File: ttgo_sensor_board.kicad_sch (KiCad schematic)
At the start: 56 parts, among them J1 Conn_01x13_Female, J2 Conn_01x13_Female, J3 Conn_01x03_Female, J4 Conn_01x03_Female, J5 Conn_01x04_Female, J6 Conn_01x04_Female, J7 Conn_01x04_Female, Q1 Q_NMOS_GSD, Q2 Q_NMOS_GSD, U1 BME680, U2 TCA9800, U3 TLV70218_SOT23-5, U4 LSM6DS3, U5 VEML7700

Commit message: backup current state
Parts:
- added TP12, TP13: TestPoint, TestPoint:TestPoint_Pad_D1.0mm, symbol Connector:TestPoint
- D3: value USER0 -> U0
- D4: value USER1 -> U1
- R2: value 290 -> 294
- TP1, TP2, TP3, TP4, TP5, TP6, TP7: footprint TestPoint:TestPoint_Pad_D1.5mm -> TestPoint:TestPoint_Pad_D1.0mm
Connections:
- net GND: no longer J2.11 (Pin_11)
- net GPIO34: now also TP12.1
- net GPIO35: now also TP13.1
- net GPIO36: no longer TP2.1
- net GPIO39: no longer TP3.1
- net VCC5: no longer J2.12 (Pin_12)
- net at Q2.3 (D), R8.1: now also TP3.1
- net at Q1.3 (D), R7.1: now also TP2.1
- new net GPIO00: J2.11 (Pin_11)
- new net GPIO04: J2.12 (Pin_12)
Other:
- moved on the sheet: TP2, TP3

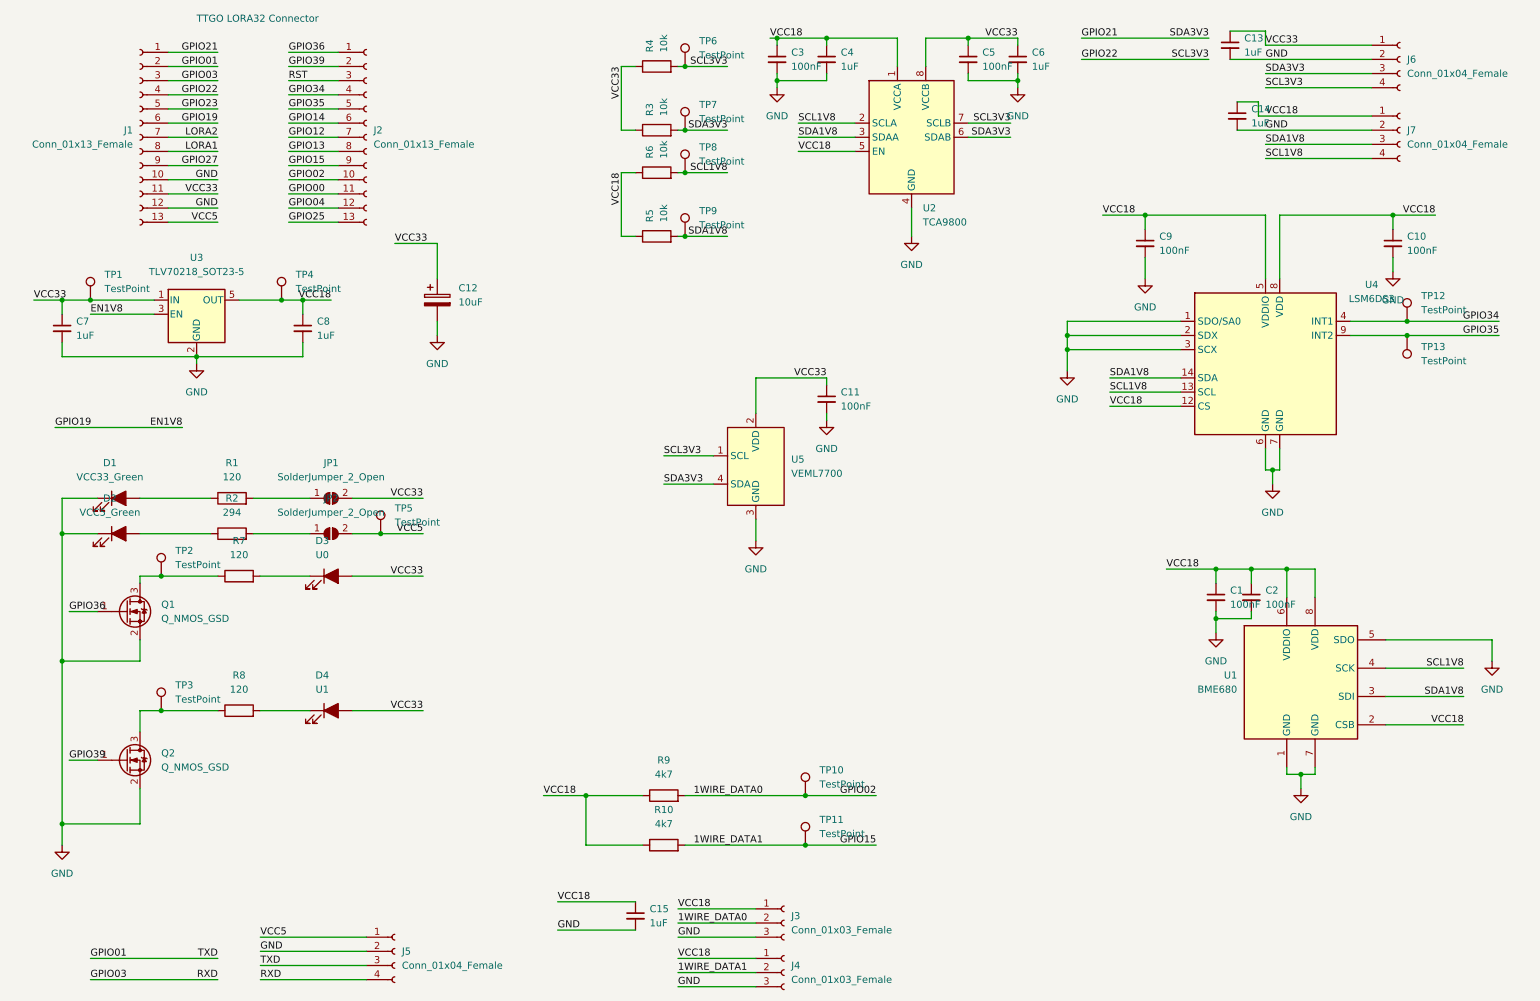
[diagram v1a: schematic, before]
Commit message: moved leds and change silkscreen
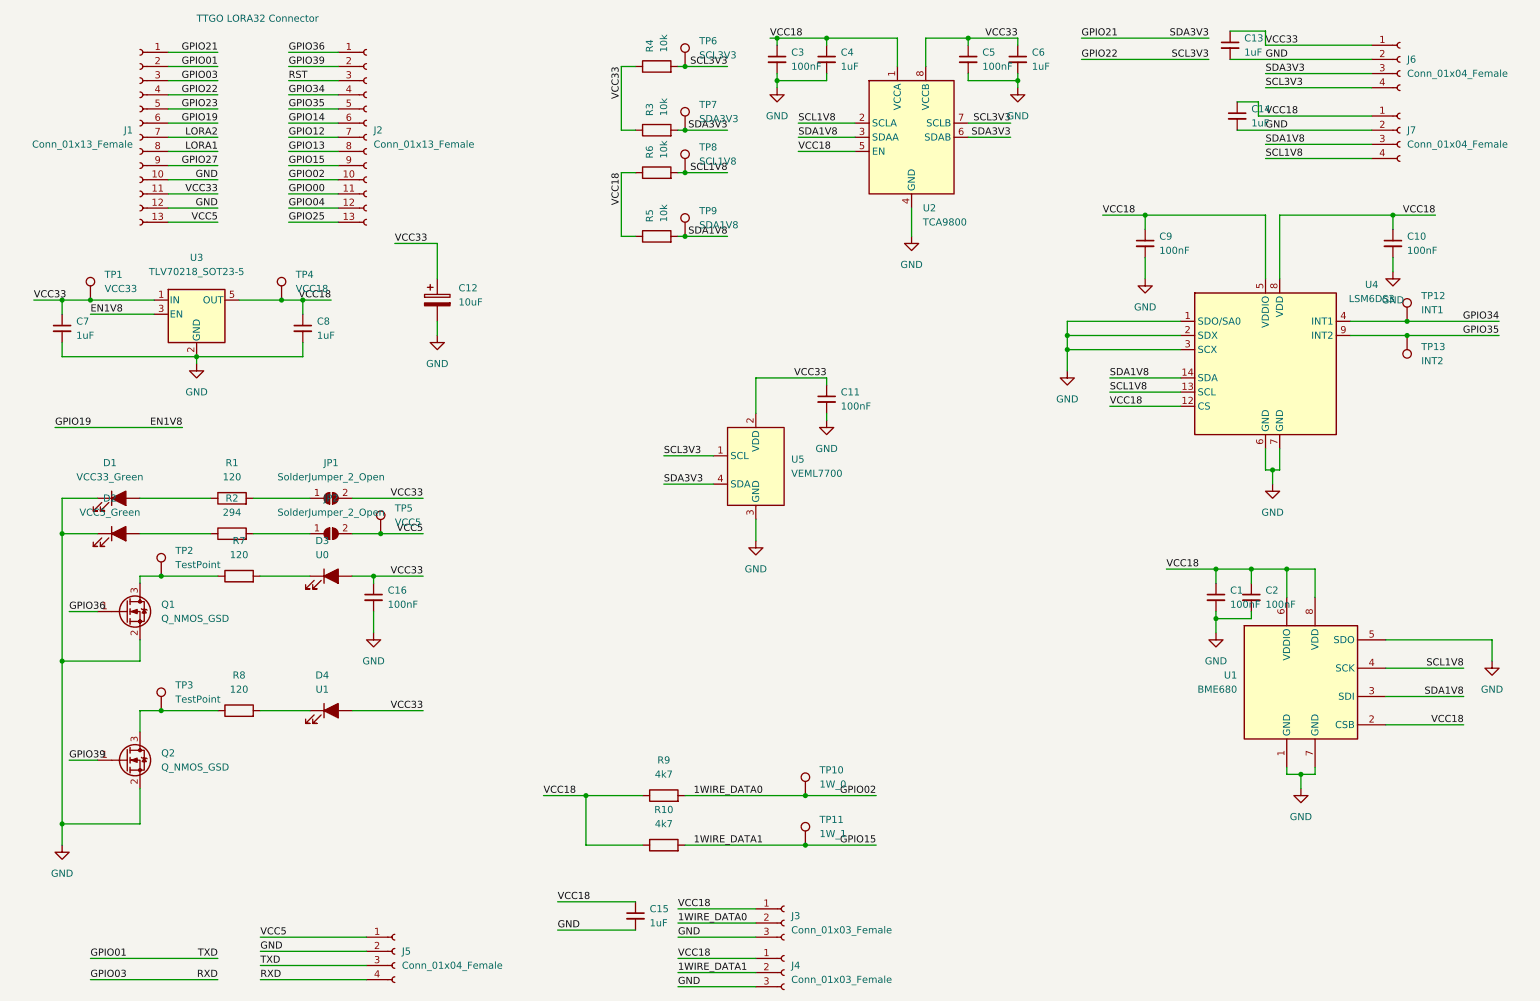
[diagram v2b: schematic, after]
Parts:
- added C16: 100nF, Capacitor_SMD:C_0603_1608Metric, symbol Device:C_Small
- TP1: value TestPoint -> VCC33
- TP10: value TestPoint -> 1W_0
- TP11: value TestPoint -> 1W_1
- TP12: value TestPoint -> INT1
- TP13: value TestPoint -> INT2
- TP4: value TestPoint -> VCC18
- TP5: value TestPoint -> VCC5
- TP6: value TestPoint -> SCL3V3
- TP7: value TestPoint -> SDA3V3
- TP8: value TestPoint -> SCL1V8
- TP9: value TestPoint -> SDA1V8
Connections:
- net GND: now also C16.2
- net VCC33: now also C16.1
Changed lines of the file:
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@@
   (junction (at 261.62 53.34) (diameter 0) (color 0 0 0 0)
   )
+  (junction (at 78.74 118.11) (diameter 0) (color 0 0 0 0)
+  )
   (junction (at 240.03 99.06) (diameter 0) (color 0 0 0 0)
   )
@@
     (stroke (width 0) (type default) (color 0 0 0 0))
   )
+  (wire (pts (xy 78.74 118.11) (xy 87.63 118.11))
+    (stroke (width 0) (type default) (color 0 0 0 0))
+  )
   (wire (pts (xy 247.65 152.4) (xy 247.65 153.67))
     (stroke (width 0) (type default) (color 0 0 0 0))
@@
     (stroke (width 0) (type default) (color 0 0 0 0))
   )
-  (wire (pts (xy 74.93 118.11) (xy 87.63 118.11))
+  (wire (pts (xy 74.93 118.11) (xy 78.74 118.11))
     (stroke (width 0) (type default) (color 0 0 0 0))
   )
@@
     (stroke (width 0) (type default) (color 0 0 0 0))
   )
+  (wire (pts (xy 78.74 118.11) (xy 78.74 119.38))
+    (stroke (width 0) (type default) (color 0 0 0 0))
+  )
   (wire (pts (xy 245.11 153.67) (xy 242.57 153.67))
     (stroke (width 0) (type default) (color 0 0 0 0))
@@
   )
   (wire (pts (xy 217.17 53.34) (xy 217.17 55.88))
+    (stroke (width 0) (type default) (color 0 0 0 0))
+  )
+  (wire (pts (xy 78.74 124.46) (xy 78.74 128.27))
     (stroke (width 0) (type default) (color 0 0 0 0))
   )
@@
     (pin "1")
     (pin "2")
+  )
+  (symbol (lib_id "power:GND") (at 78.74 128.27 0) (unit 1)
+    (in_bom yes) (on_board yes) (fields_autoplaced)
+    (property "Reference" "#PWR016" (id 0) (at 78.74 134.62 0)
+      (effects (font (size 1.27 1.27)) hide)
+    )
+    (property "Value" "GND" (id 1) (at 78.74 133.35 0))
+    (property "Footprint" "" (id 2) (at 78.74 128.27 0)
+      (effects (font (size 1.27 1.27)) hide)
+    )
+    (property "Datasheet" "" (id 3) (at 78.74 128.27 0)
+      (effects (font (size 1.27 1.27)) hide)
+    )
+    (pin "1")
   )
   (symbol (lib_id "Device:R") (at 129.54 45.72 90) (unit 1)
@@
       (effects (font (size 1.27 1.27)) (justify left))
     )
-    (property "Value" "TestPoint" (id 1) (at 158.75 155.4479 0)
+    (property "Value" "1W_0" (id 1) (at 158.75 155.4479 0)
       (effects (font (size 1.27 1.27)) (justify left))
     )
@@
       (effects (font (size 1.27 1.27)) (justify left))
     )
-    (property "Value" "TestPoint" (id 1) (at 158.75 164.3379 0)
+    (property "Value" "1W_1" (id 1) (at 158.75 164.3379 0)
       (effects (font (size 1.27 1.27)) (justify left))
     )
@@
       (effects (font (size 1.27 1.27)) (justify left))
     )
-    (property "Value" "TestPoint" (id 1) (at 64.77 66.5479 0)
+    (property "Value" "VCC18" (id 1) (at 64.77 66.5479 0)
       (effects (font (size 1.27 1.27)) (justify left))
     )
@@
       (effects (font (size 1.27 1.27)) (justify left))
     )
-    (property "Value" "TestPoint" (id 1) (at 137.16 24.6379 0)
+    (property "Value" "SCL3V3" (id 1) (at 137.16 24.6379 0)
       (effects (font (size 1.27 1.27)) (justify left))
     )
@@
     (pin "3")
   )
+  (symbol (lib_id "Device:C_Small") (at 78.74 121.92 0) (unit 1)
+    (in_bom yes) (on_board yes) (fields_autoplaced)
+    (property "Reference" "C16" (id 0) (at 81.28 120.6562 0)
+      (effects (font (size 1.27 1.27)) (justify left))
+    )
+    (property "Value" "100nF" (id 1) (at 81.28 123.1962 0)
+      (effects (font (size 1.27 1.27)) (justify left))
+    )
+    (property "Footprint" "Capacitor_SMD:C_0603_1608Metric" (id 2) (at 78.74 121.92 0)
+      (effects (font (size 1.27 1.27)) hide)
+    )
+    (property "Datasheet" "~" (id 3) (at 78.74 121.92 0)
+      (effects (font (size 1.27 1.27)) hide)
+    )
+    (pin "1")
+    (pin "2")
+  )
   (symbol (lib_id "Device:C_Small") (at 236.22 121.92 0) (unit 1)
     (in_bom yes) (on_board yes) (fields_autoplaced)
@@
       (effects (font (size 1.27 1.27)) (justify right))
     )
-    (property "Value" "TestPoint" (id 1) (at 266.7 79.5019 0)
+    (property "Value" "INT2" (id 1) (at 266.7 79.5019 0)
       (effects (font (size 1.27 1.27)) (justify right))
     )
@@
       (effects (font (size 1.27 1.27)) (justify left))
     )
-    (property "Value" "TestPoint" (id 1) (at 137.16 43.6879 0)
+    (property "Value" "SCL1V8" (id 1) (at 137.16 43.6879 0)
       (effects (font (size 1.27 1.27)) (justify left))
     )
@@
       (effects (font (size 1.27 1.27)) (justify left))
     )
-    (property "Value" "TestPoint" (id 1) (at 30.48 66.5479 0)
+    (property "Value" "VCC33" (id 1) (at 30.48 66.5479 0)
       (effects (font (size 1.27 1.27)) (justify left))
     )
@@
       (effects (font (size 1.27 1.27)) (justify left))
     )
-    (property "Value" "TestPoint" (id 1) (at 137.16 55.1179 0)
+    (property "Value" "SDA1V8" (id 1) (at 137.16 55.1179 0)
       (effects (font (size 1.27 1.27)) (justify left))
     )
@@
       (effects (font (size 1.27 1.27)) (justify left))
     )
-    (property "Value" "TestPoint" (id 1) (at 266.7 70.3579 0)
+    (property "Value" "INT1" (id 1) (at 266.7 70.3579 0)
       (effects (font (size 1.27 1.27)) (justify left))
     )
@@
       (effects (font (size 1.27 1.27)) (justify left))
     )
-    (property "Value" "TestPoint" (id 1) (at 137.16 36.0679 0)
+    (property "Value" "SDA3V3" (id 1) (at 137.16 36.0679 0)
       (effects (font (size 1.27 1.27)) (justify left))
     )
@@
       (effects (font (size 1.27 1.27)) (justify left))
     )
-    (property "Value" "TestPoint" (id 1) (at 82.55 108.4579 0)
+    (property "Value" "VCC5" (id 1) (at 82.55 108.4579 0)
       (effects (font (size 1.27 1.27)) (justify left))
     )
@@
       (reference "#PWR015") (unit 1) (value "GND") (footprint "")
     )
+    (path "/120c1b77-b148-4401-99a1-eb6dd5ecad45"
+      (reference "#PWR016") (unit 1) (value "GND") (footprint "")
+    )
     (path "/303bc827-9cd2-440d-a75f-903becfea595"
       (reference "C1") (unit 1) (value "100nF") (footprint "Capacitor_SMD:C_0603_1608Metric")
@@
       (reference "C15") (unit 1) (value "1uF") (footprint "Capacitor_SMD:C_0805_2012Metric")
     )
+    (path "/6e51b006-ab44-4e64-8079-8c4d9ab501ce"
+      (reference "C16") (unit 1) (value "100nF") (footprint "Capacitor_SMD:C_0603_1608Metric")
+    )
     (path "/7798c7e6-7915-4a6b-ab42-a766ebbf3ea2"
       (reference "D1") (unit 1) (value "VCC33_Green") (footprint "LED_SMD:LED_0603_1608Metric")
@@
     )
     (path "/bcde0377-8c26-4b69-8954-a51a2ffb793f"
-      (reference "TP1") (unit 1) (value "TestPoint") (footprint "TestPoint:TestPoint_Pad_D1.0mm")
+      (reference "TP1") (unit 1) (value "VCC33") (footprint "TestPoint:TestPoint_Pad_D1.0mm")
     )
     (path "/3da8c133-6711-4639-b750-4f849ed621b0"
@@
     )
     (path "/466255f5-b832-450e-919d-5e3de13155b2"
-      (reference "TP4") (unit 1) (value "TestPoint") (footprint "TestPoint:TestPoint_Pad_D1.0mm")
+      (reference "TP4") (unit 1) (value "VCC18") (footprint "TestPoint:TestPoint_Pad_D1.0mm")
     )
     (path "/f8cddcce-59f6-46d6-93f1-ff47f4225b00"
-      (reference "TP5") (unit 1) (value "TestPoint") (footprint "TestPoint:TestPoint_Pad_D1.0mm")
+      (reference "TP5") (unit 1) (value "VCC5") (footprint "TestPoint:TestPoint_Pad_D1.0mm")
     )
     (path "/54deacdd-7ba1-4627-bd7b-8cb63ddf4fdd"
-      (reference "TP6") (unit 1) (value "TestPoint") (footprint "TestPoint:TestPoint_Pad_D1.0mm")
+      (reference "TP6") (unit 1) (value "SCL3V3") (footprint "TestPoint:TestPoint_Pad_D1.0mm")
     )
     (path "/df02339f-b53e-463e-8ca2-0979e87e04fa"
-      (reference "TP7") (unit 1) (value "TestPoint") (footprint "TestPoint:TestPoint_Pad_D1.0mm")
+      (reference "TP7") (unit 1) (value "SDA3V3") (footprint "TestPoint:TestPoint_Pad_D1.0mm")
     )
     (path "/90daf277-2570-45af-b223-fef70d586fac"
-      (reference "TP8") (unit 1) (value "TestPoint") (footprint "TestPoint:TestPoint_Pad_D1.0mm")
+      (reference "TP8") (unit 1) (value "SCL1V8") (footprint "TestPoint:TestPoint_Pad_D1.0mm")
     )
     (path "/ce65b3d7-77a6-4f25-aa8d-7656509a970f"
-      (reference "TP9") (unit 1) (value "TestPoint") (footprint "TestPoint:TestPoint_Pad_D1.0mm")
+      (reference "TP9") (unit 1) (value "SDA1V8") (footprint "TestPoint:TestPoint_Pad_D1.0mm")
     )
     (path "/1bf7c139-7bd4-4fe2-9d9b-e84962e73ab6"
-      (reference "TP10") (unit 1) (value "TestPoint") (footprint "TestPoint:TestPoint_Pad_D1.0mm")
+      (reference "TP10") (unit 1) (value "1W_0") (footprint "TestPoint:TestPoint_Pad_D1.0mm")
     )
     (path "/2a038efe-0895-47e8-a66b-4538c755a9d4"
-      (reference "TP11") (unit 1) (value "TestPoint") (footprint "TestPoint:TestPoint_Pad_D1.0mm")
+      (reference "TP11") (unit 1) (value "1W_1") (footprint "TestPoint:TestPoint_Pad_D1.0mm")
     )
     (path "/d6fe46a3-86ab-4a02-b877-c9c2ae2ca582"
-      (reference "TP12") (unit 1) (value "TestPoint") (footprint "TestPoint:TestPoint_Pad_D1.0mm")
+      (reference "TP12") (unit 1) (value "INT1") (footprint "TestPoint:TestPoint_Pad_D1.0mm")
     )
     (path "/88b03a15-6b2d-4ef3-9fe0-64296a19b3d9"
-      (reference "TP13") (unit 1) (value "TestPoint") (footprint "TestPoint:TestPoint_Pad_D1.0mm")
+      (reference "TP13") (unit 1) (value "INT2") (footprint "TestPoint:TestPoint_Pad_D1.0mm")
     )
     (path "/c96b559d-9826-4579-b5bb-64fc3d452210"

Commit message: production state
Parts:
- R2: value 294 -> 300
- R7, R8: value 120 -> 82
- TP2: value TestPoint -> USER0
- TP3: value TestPoint -> USER1
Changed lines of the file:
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@@
     (in_bom yes) (on_board yes)
     (property "Reference" "R8" (id 0) (at 54.61 135.89 90))
-    (property "Value" "120" (id 1) (at 54.61 138.43 90))
+    (property "Value" "82" (id 1) (at 54.61 138.43 90))
     (property "Footprint" "Resistor_SMD:R_0603_1608Metric" (id 2) (at 54.61 144.018 90)
       (effects (font (size 1.27 1.27)) hide)
@@
     (in_bom yes) (on_board yes) (fields_autoplaced)
     (property "Reference" "R7" (id 0) (at 54.61 111.76 90))
-    (property "Value" "120" (id 1) (at 54.61 114.3 90))
+    (property "Value" "82" (id 1) (at 54.61 114.3 90))
     (property "Footprint" "Resistor_SMD:R_0603_1608Metric" (id 2) (at 54.61 119.888 90)
       (effects (font (size 1.27 1.27)) hide)
@@
       (effects (font (size 1.27 1.27)) (justify left))
     )
-    (property "Value" "TestPoint" (id 1) (at 43.18 116.0779 0)
+    (property "Value" "USER0" (id 1) (at 43.18 116.0779 0)
       (effects (font (size 1.27 1.27)) (justify left))
     )
@@
       (effects (font (size 1.27 1.27)) (justify left))
     )
-    (property "Value" "TestPoint" (id 1) (at 43.18 140.2079 0)
+    (property "Value" "USER1" (id 1) (at 43.18 140.2079 0)
       (effects (font (size 1.27 1.27)) (justify left))
     )
@@
     (in_bom yes) (on_board yes) (fields_autoplaced)
     (property "Reference" "R2" (id 0) (at 53.34 104.14 90))
-    (property "Value" "294" (id 1) (at 53.34 106.68 90))
+    (property "Value" "300" (id 1) (at 53.34 106.68 90))
     (property "Footprint" "Resistor_SMD:R_0603_1608Metric" (id 2) (at 53.34 112.268 90)
       (effects (font (size 1.27 1.27)) hide)
@@
     )
     (path "/de0ebb11-8d49-4b76-822b-99543b6eed0f"
-      (reference "R2") (unit 1) (value "294") (footprint "Resistor_SMD:R_0603_1608Metric")
+      (reference "R2") (unit 1) (value "300") (footprint "Resistor_SMD:R_0603_1608Metric")
     )
     (path "/269a132c-8f66-4ed5-9a32-4e13b0b1de9b"
@@
     )
     (path "/1a764047-a80f-48fa-9356-557bc7ba61b6"
-      (reference "R7") (unit 1) (value "120") (footprint "Resistor_SMD:R_0603_1608Metric")
+      (reference "R7") (unit 1) (value "82") (footprint "Resistor_SMD:R_0603_1608Metric")
     )
     (path "/0cb21074-c045-48f6-8743-4c268a62950d"
-      (reference "R8") (unit 1) (value "120") (footprint "Resistor_SMD:R_0603_1608Metric")
+      (reference "R8") (unit 1) (value "82") (footprint "Resistor_SMD:R_0603_1608Metric")
     )
     (path "/be5bd9b5-3fb2-4be7-a3d2-60d82020931f"
@@
     )
     (path "/3da8c133-6711-4639-b750-4f849ed621b0"
-      (reference "TP2") (unit 1) (value "TestPoint") (footprint "TestPoint:TestPoint_Pad_D1.0mm")
+      (reference "TP2") (unit 1) (value "USER0") (footprint "TestPoint:TestPoint_Pad_D1.0mm")
     )
     (path "/7284972f-69e3-48ac-ba8a-b45c6ce11ed6"
-      (reference "TP3") (unit 1) (value "TestPoint") (footprint "TestPoint:TestPoint_Pad_D1.0mm")
+      (reference "TP3") (unit 1) (value "USER1") (footprint "TestPoint:TestPoint_Pad_D1.0mm")
     )
     (path "/466255f5-b832-450e-919d-5e3de13155b2"
